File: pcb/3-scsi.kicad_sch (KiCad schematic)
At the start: 71 parts, among them J301 IDC50 box header, J302 HD50 female R/A, J303 2x17 box header, SW301 DIP 2-pos, U301 SN74LVTH245APWR, U302 SN74LVTH245APWR, U303 SN74LVTH245APWR

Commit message: almost completely routed
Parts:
- added R1, R2, R3, R4: 0R, Resistor_SMD:R_0402_1005Metric, symbol Device:R
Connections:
- net GND: now also R1.2, R2.2, R3.2, R4.2
- net LOGIC_ANALYZER_MARKER0: now also J303.3 (Pin_3); no longer J303.5 (Pin_5)
- net LOGIC_ANALYZER_MARKER1: now also J303.5 (Pin_5); no longer J303.3 (Pin_3)
- net SCSI_RESERVED_23: no longer J302.12 (Pin_12)
- net SCSI_RESERVED_24: no longer J302.37 (Pin_37)
- net SCSI_RESERVED_27: no longer J302.14 (Pin_14)
- net SCSI_RESERVED_28: no longer J302.39 (Pin_39)
- new net SCSI_RESERVED_23_hd50: J302.12 (Pin_12), R1.1
- new net SCSI_RESERVED_24_hd50: J302.37 (Pin_37), R2.1
- new net SCSI_RESERVED_27_hd50: J302.14 (Pin_14), R3.1
- new net SCSI_RESERVED_28_hd50: J302.39 (Pin_39), R4.1

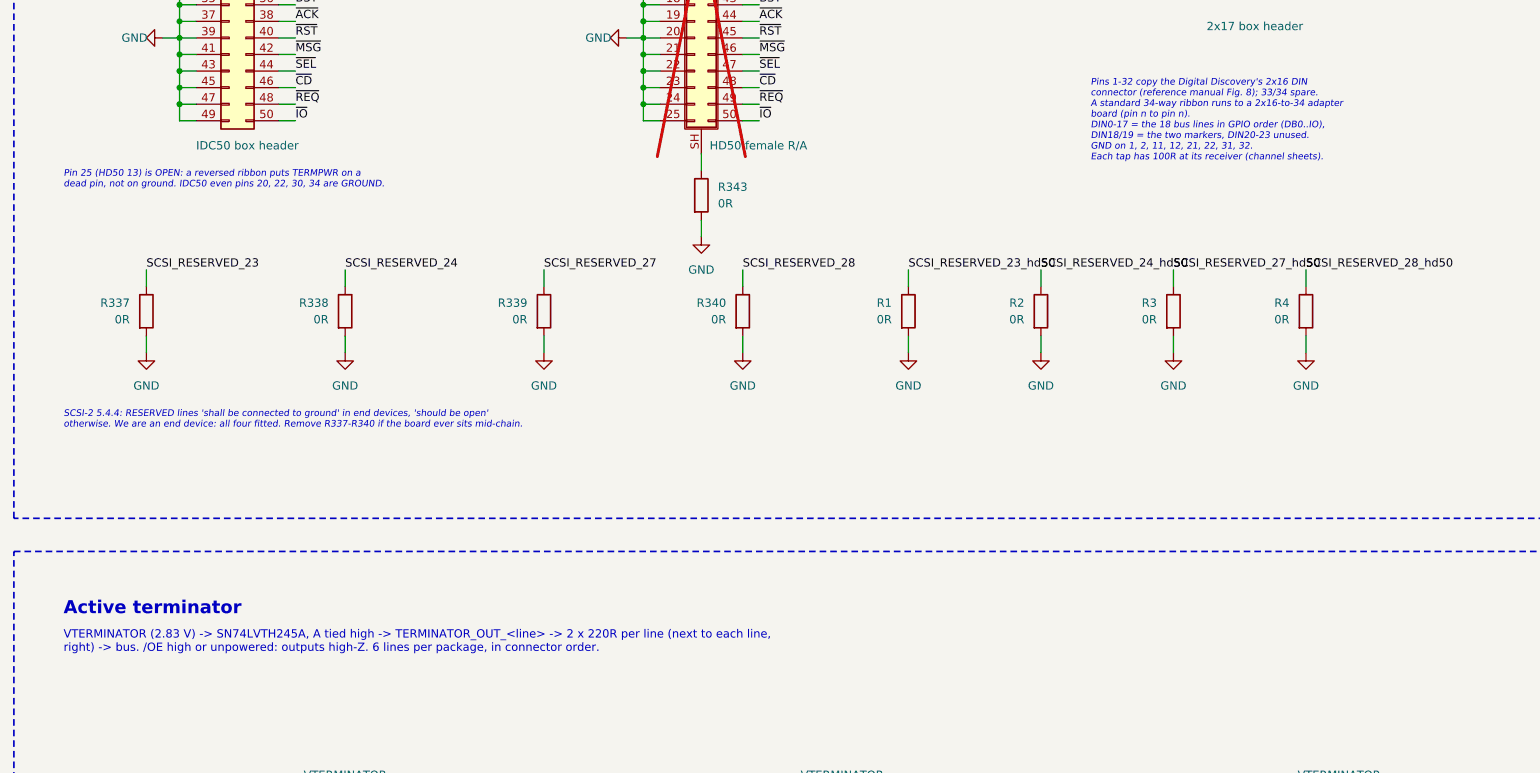
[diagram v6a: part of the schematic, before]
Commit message: reorder passives near ft232h
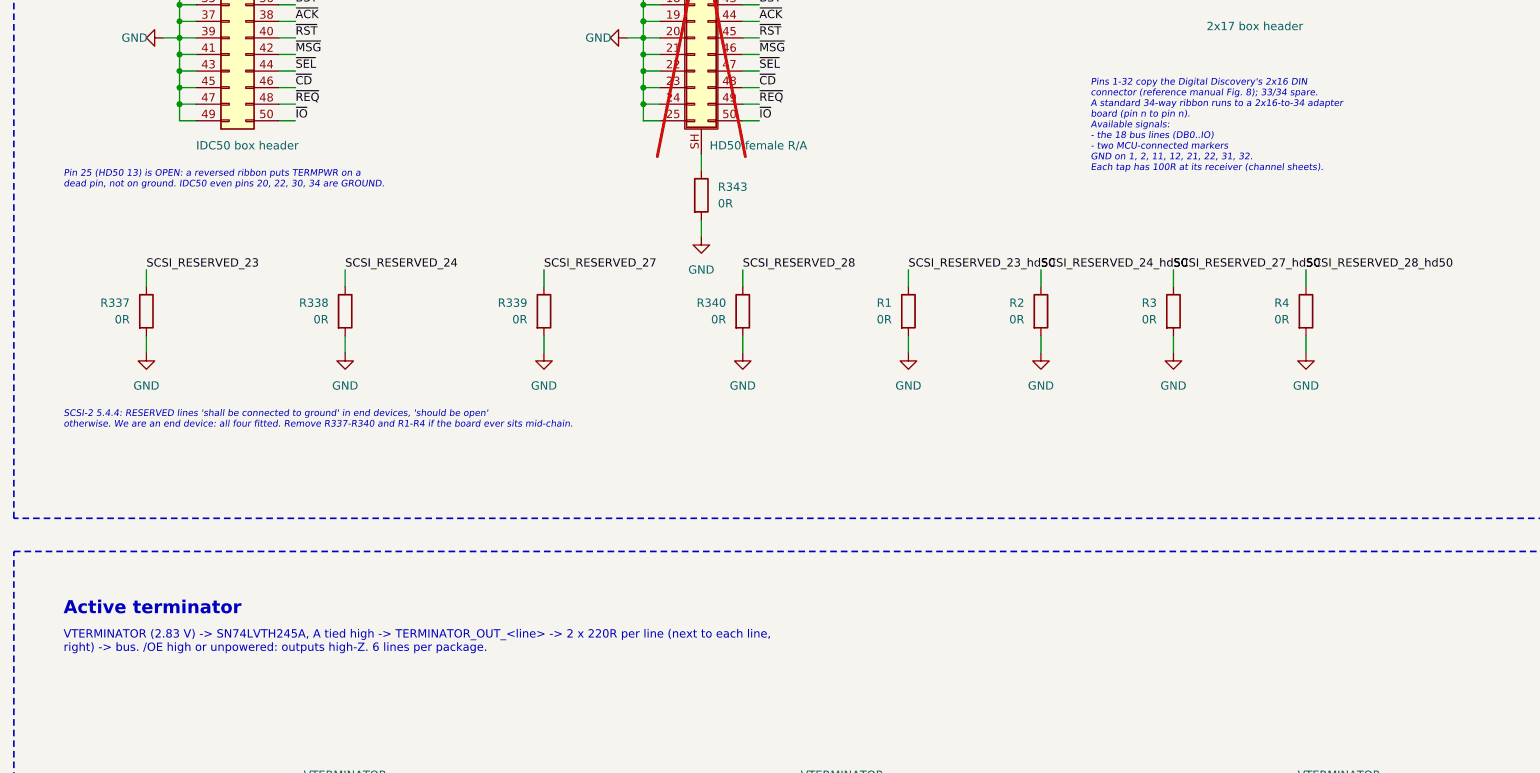
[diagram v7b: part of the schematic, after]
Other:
- note added: "Pins 1-32 copy the Digital Discovery's 2x16 DIN connector (reference manual Fig. 8); 33/34 spare. A standard 34-way ribbon runs to a 2x16-to-34 adapter board (pin n to pin n). Available signals: - the 18 bus lines (DB0..IO) - two MCU-connected markers GND on 1, 2, 11, 12, 21, 22, 31, 32. Each tap has 100R at its receiver (channel sheets)."
- note added: "SCSI-2 5.4.4: RESERVED lines 'shall be connected to ground' in end devices, 'should be open' otherwise. We are an end device: all four fitted. Remove R337-R340 and R1-R4 if the board ever sits mid-chain."
- note added: "VTERMINATOR (2.83 V) -> SN74LVTH245A, A tied high -> TERMINATOR_OUT_<line> -> 2 x 220R per line (next to each line, right) -> bus. /OE high or unpowered: outputs high-Z. 6 lines per package."
- note removed: "Pins 1-32 copy the Digital Discovery's 2x16 DIN connector (reference manual Fig. 8); 33/34 spare. A standard 34-way ribbon runs to a 2x16-to-34 adapter board (pin n to pin n). DIN0-17 = the 18 bus lines in GPIO order (DB0..IO), DIN18/19 = the two markers, DIN20-23 unused. GND on 1, 2, 11, 12, 21, 22, 31, 32. Each tap has 100R at its receiver (channel sheets)."
- note removed: "SCSI-2 5.4.4: RESERVED lines 'shall be connected to ground' in end devices, 'should be open' otherwise. We are an end device: all four fitted. Remove R337-R340 if the board ever sits mid-chain."
- note removed: "VTERMINATOR (2.83 V) -> SN74LVTH245A, A tied high -> TERMINATOR_OUT_<line> -> 2 x 220R per line (next to each line, right) -> bus. /OE high or unpowered: outputs high-Z. 6 lines per package, in connector order."
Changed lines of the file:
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@@
 		)
 	)
-	(text "Pins 1-32 copy the Digital Discovery's 2x16 DIN\nconnector (reference manual Fig. 8); 33/34 spare.\nA standard 34-way ribbon runs to a 2x16-to-34 adapter\nboard (pin n to pin n).\nDIN0-17 = the 18 bus lines in GPIO order (DB0..IO),\nDIN18/19 = the two markers, DIN20-23 unused.\nGND on 1, 2, 11, 12, 21, 22, 31, 32.\nEach tap has 100R at its receiver (channel sheets)."
+	(text "Pins 1-32 copy the Digital Discovery's 2x16 DIN\nconnector (reference manual Fig. 8); 33/34 spare.\nA standard 34-way ribbon runs to a 2x16-to-34 adapter\nboard (pin n to pin n).\nAvailable signals:\n- the 18 bus lines (DB0..IO)\n- two MCU-connected markers\nGND on 1, 2, 11, 12, 21, 22, 31, 32.\nEach tap has 100R at its receiver (channel sheets)."
 		(exclude_from_sim no)
 		(at 177.8 100.33 0)
@@
 		)
 	)
-	(text "SCSI-2 5.4.4: RESERVED lines 'shall be connected to ground' in end devices, 'should be open'\notherwise. We are an end device: all four fitted. Remove R337-R340 if the board ever sits mid-chain."
+	(text "SCSI-2 5.4.4: RESERVED lines 'shall be connected to ground' in end devices, 'should be open'\notherwise. We are an end device: all four fitted. Remove R337-R340 and R1-R4 if the board ever sits mid-chain."
 		(exclude_from_sim no)
 		(at 20.32 151.13 0)
@@
 		)
 	)
-	(text "VTERMINATOR (2.83 V) -> SN74LVTH245A, A tied high -> TERMINATOR_OUT_<line> -> 2 x 220R per line (next to each line,\nright) -> bus. /OE high or unpowered: outputs high-Z. 6 lines per package, in connector order."
+	(text "VTERMINATOR (2.83 V) -> SN74LVTH245A, A tied high -> TERMINATOR_OUT_<line> -> 2 x 220R per line (next to each line,\nright) -> bus. /OE high or unpowered: outputs high-Z. 6 lines per package."
 		(exclude_from_sim no)
 		(at 20.32 184.84 0)
